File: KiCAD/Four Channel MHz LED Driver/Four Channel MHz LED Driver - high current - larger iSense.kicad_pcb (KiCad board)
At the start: 2 copper layers, 100 x 126 mm, 85 parts, among them J10 Conn_01x24_Female, J2 Conn_01x02_Female, J3 8P8C_Shielded_x4, J4 Conn_01x03_Male, J5 Conn_01x03_Female, J6 Conn_01x08_Female, J7 Conn_01x03_Female, J8 Conn_01x05_Female, J9 Conn_01x24_Female, M1 Fan_4pin, Q1 SUM70060E, SW1 Pushbutton_with_LED, SW2 Pushbutton_with_LED, SW3 Pushbutton_with_LED, SW4 Pushbutton_with_LED, SW5 SW_SPDT, U1 12V boost, U12 Teensy3.6, U2 SN74LV4T125PWR, U3 DPBW06F-05, U4 TMUX1204DGSR, U5 HTSOP-J8_ROM, U6 ADP7182AUJZ-1.8-R7, U7 LT6200CS8-10

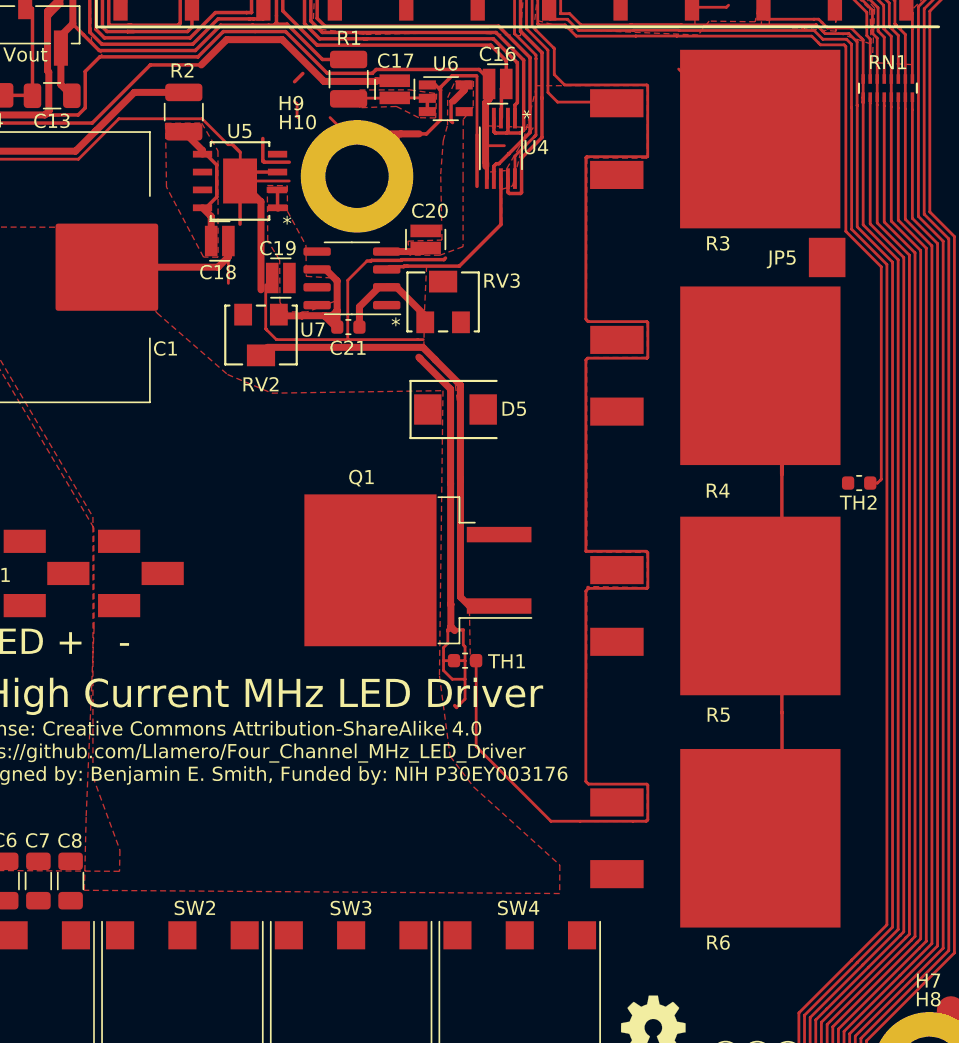
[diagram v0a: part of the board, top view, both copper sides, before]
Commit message: high power resistor pads - wide pours
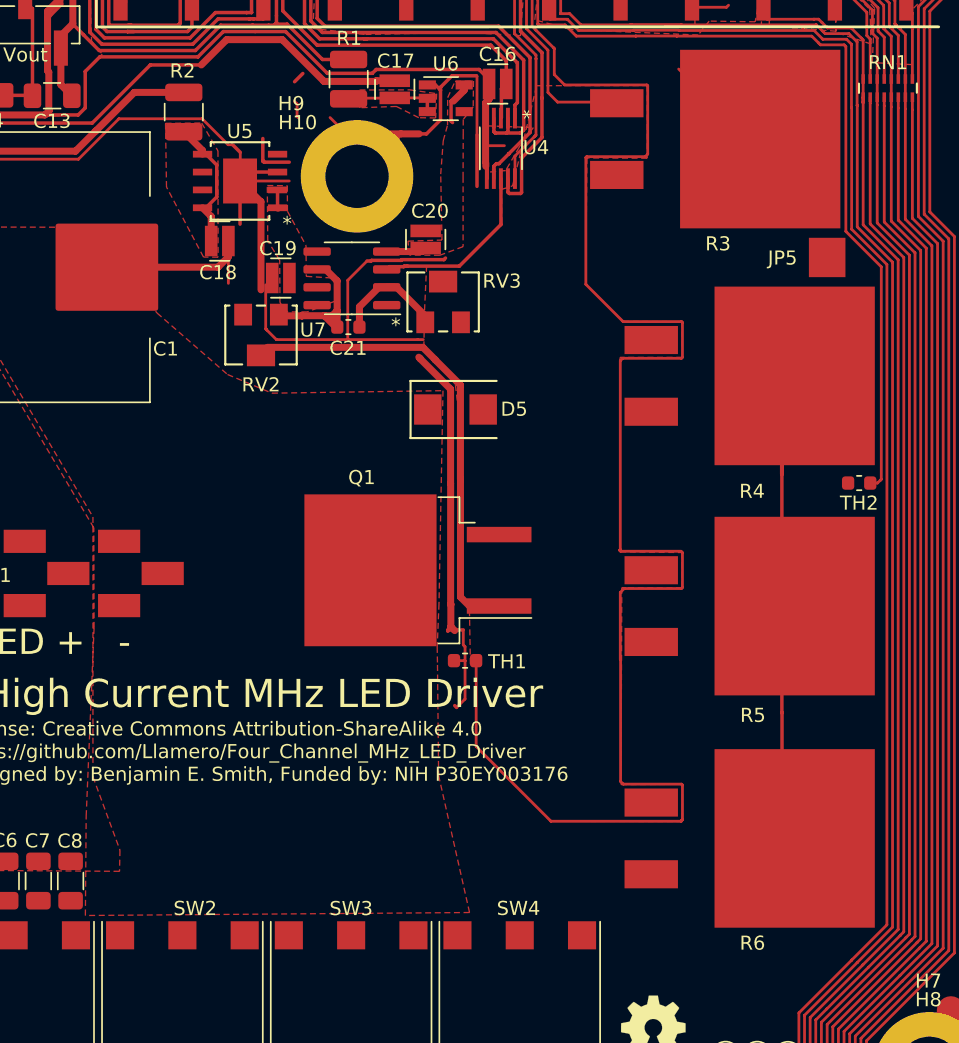
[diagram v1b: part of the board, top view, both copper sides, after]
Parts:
- moved R4 2.44 mm to (144.2, 113.0)
- moved R5 2.44 mm to (144.2, 129.4)
- moved R6 2.44 mm to (144.2, 145.9)
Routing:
- net /MOSFET_temp: track 157.6 -> 160.7 mm
- net GND: track 873.7 -> 873.2 mm
